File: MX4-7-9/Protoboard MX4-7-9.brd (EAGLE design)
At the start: 82.7 x 59.4 mm, 444 parts, among them J1 DCJ0202

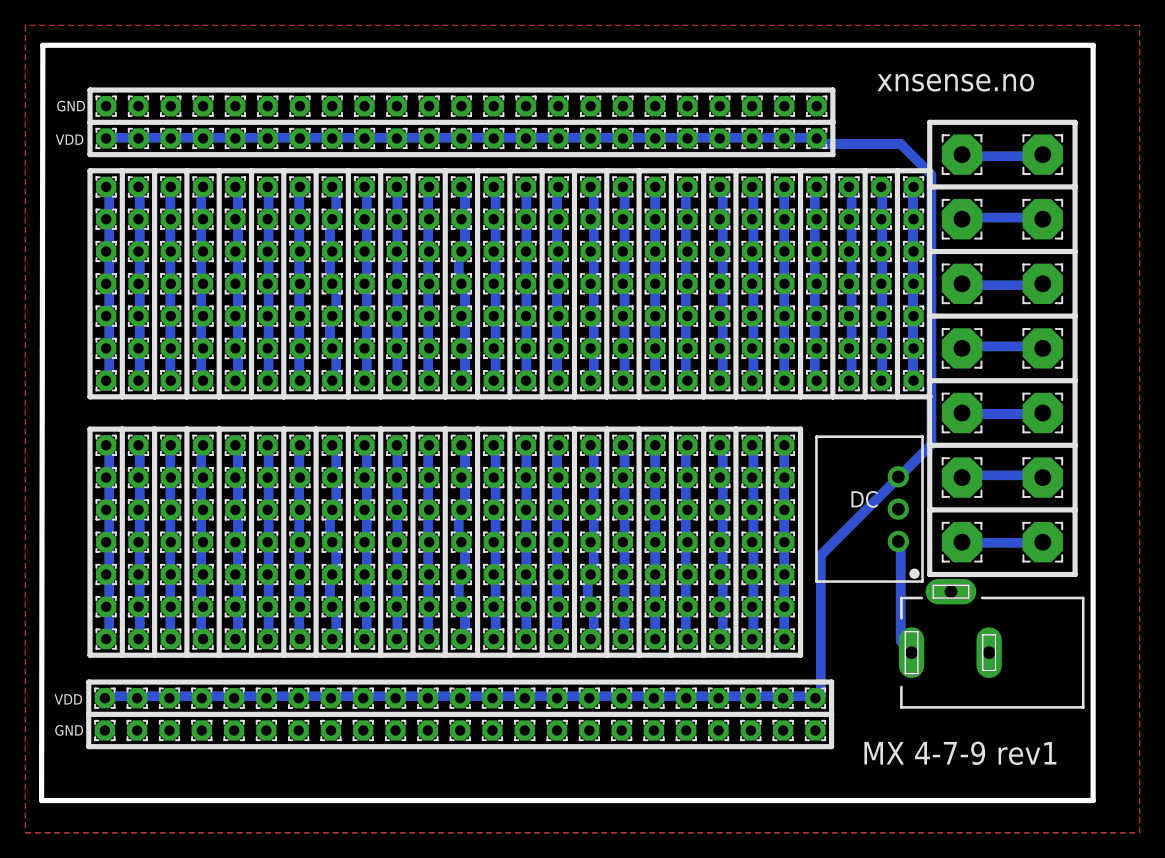
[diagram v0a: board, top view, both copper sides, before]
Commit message: Adjusted Polygon
Adjusted Polygon on all boxes. Changed length on MX-4-7-6 to fit the
box, it was 2mm to long.
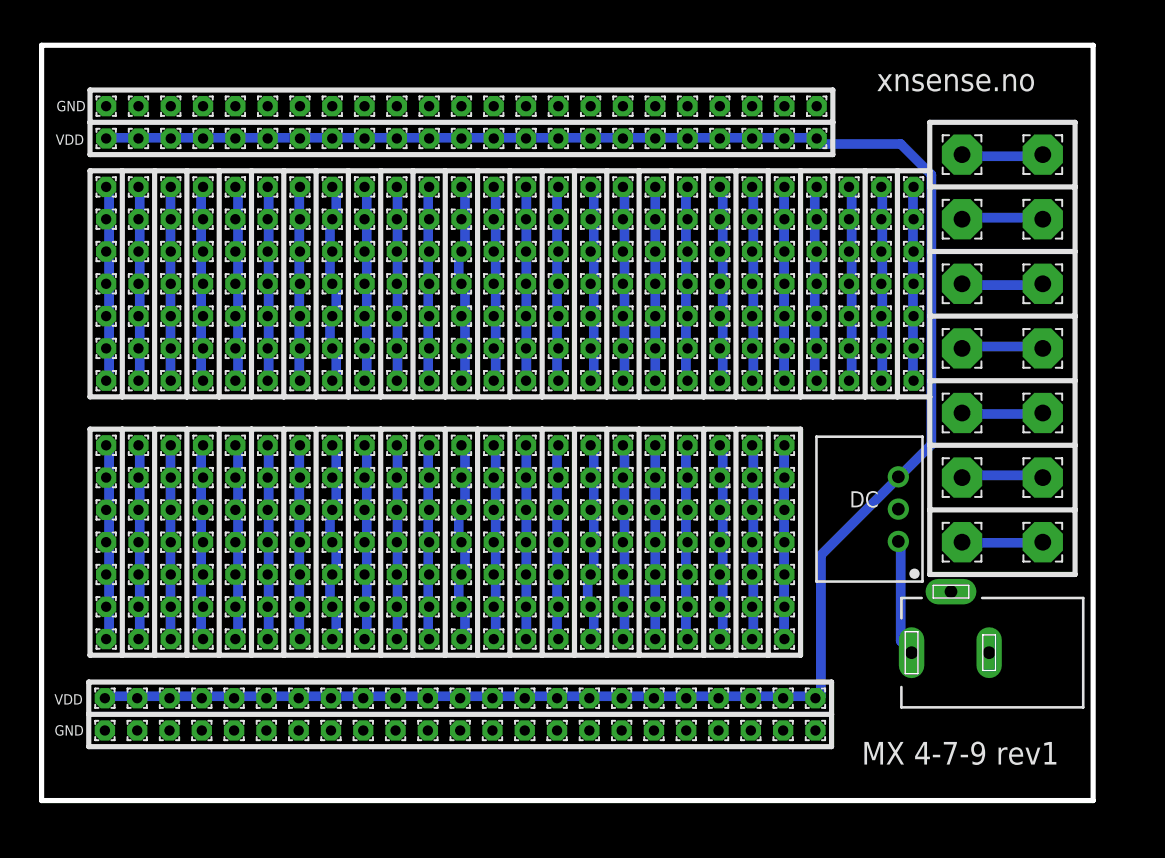
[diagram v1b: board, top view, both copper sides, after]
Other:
- outline, holes or cut-outs redrawn
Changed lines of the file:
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@@
 <?xml version="1.0" encoding="utf-8"?>
 <!DOCTYPE eagle SYSTEM "eagle.dtd">
-<eagle version="7.6.0">
+<eagle version="7.7.0">
 <drawing>
 <settings>
@@
 <setting verticaltext="up"/>
 </settings>
-<grid distance="1.27" unitdist="mm" unit="mm" style="dots" multiple="1" display="yes" altdistance="0.1" altunitdist="mm" altunit="mm"/>
+<grid distance="1.27" unitdist="mm" unit="mil" style="dots" multiple="1" display="yes" altdistance="25" altunitdist="mil" altunit="mil"/>
 <layers>
 <layer number="1" name="Top" color="4" fill="1" visible="yes" active="yes"/>
@@
 <board>
 <plain>
-<wire x1="0" y1="0" x2="0.1" y2="59.4" width="0.4064" layer="20"/>
+<wire x1="0" y1="0" x2="0" y2="59.4" width="0.4064" layer="20"/>
 <wire x1="0" y1="0" x2="82.7" y2="0" width="0.4064" layer="20"/>
-<wire x1="82.7" y1="59.4" x2="0.1" y2="59.4" width="0.4064" layer="20"/>
+<wire x1="82.7" y1="59.4" x2="0" y2="59.4" width="0.4064" layer="20"/>
 <wire x1="82.7" y1="59.4" x2="82.7" y2="0" width="0.4064" layer="20"/>
 <wire x1="44.45" y1="49.53" x2="44.45" y2="31.75" width="0.4064" layer="25"/>
@@
 <contactref element="DC" pad="2"/>
 <polygon width="0.4064" layer="1">
-<vertex x="-1.27" y="60.96"/>
-<vertex x="-1.27" y="-2.54"/>
-<vertex x="86.36" y="-2.54"/>
-<vertex x="86.36" y="60.96"/>
+<vertex x="0" y="59.4"/>
+<vertex x="0" y="0"/>
+<vertex x="82.7" y="0"/>
+<vertex x="82.7" y="59.4"/>
 </polygon>
 <contactref element="PAD27" pad="1"/>

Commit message: Update to rev2
Updated to Pin headers instead of single wire pads
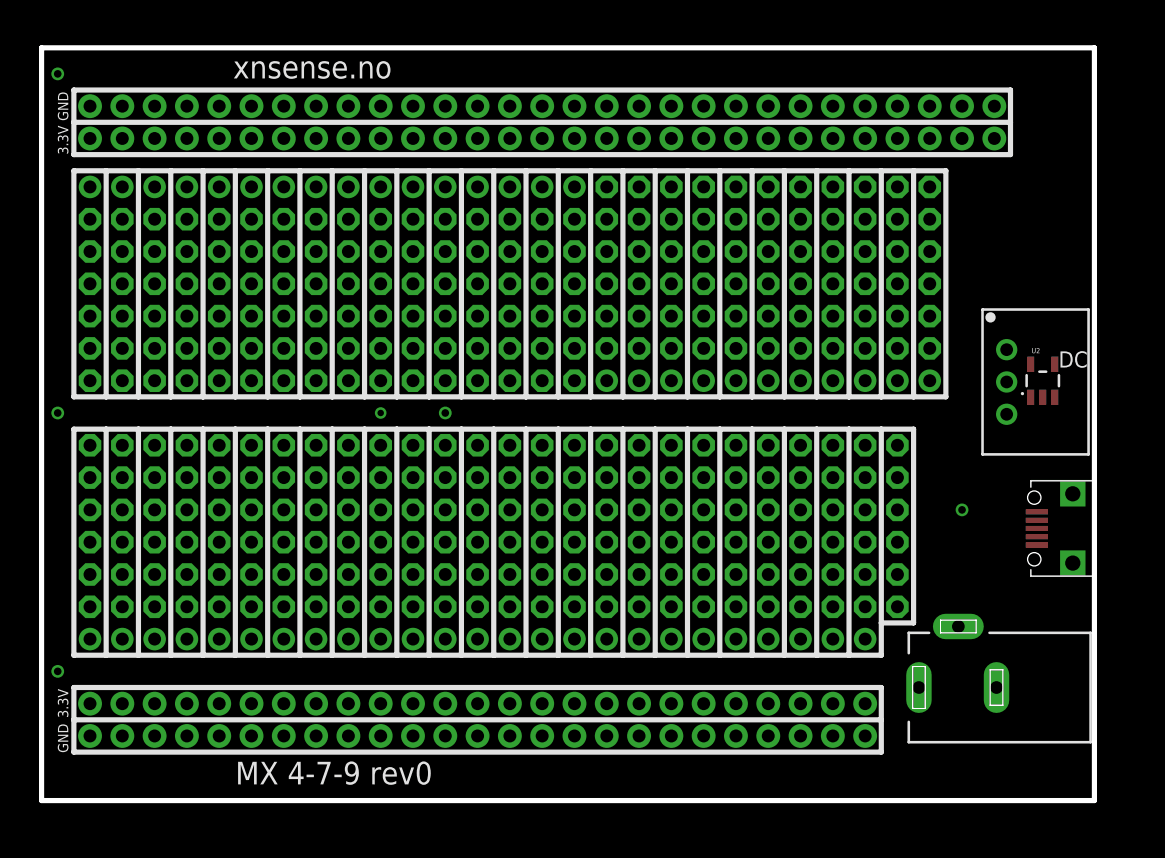
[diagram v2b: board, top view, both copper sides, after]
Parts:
- removed PAD1, PAD10, PAD100, PAD101, PAD102, PAD103, PAD104, PAD105, PAD106, PAD107, PAD108, PAD109, PAD11, PAD110, PAD111, PAD112, PAD113, PAD114, PAD115, PAD116, PAD117, PAD118, PAD119, PAD12, PAD120, PAD121, PAD122, PAD123, PAD124, PAD125, PAD126, PAD127, PAD128, PAD129, PAD13, PAD130, PAD131, PAD132, PAD133, PAD134, PAD135, PAD136, PAD137, PAD138, PAD139, PAD14, PAD140, PAD141, PAD142, PAD143, PAD144, PAD145, PAD146, PAD147, PAD148, PAD149, PAD15, PAD150, PAD151, PAD152, PAD153, PAD154, PAD155, PAD156, PAD157, PAD158, PAD159, PAD16, PAD160, PAD161, PAD162, PAD163, PAD164, PAD165, PAD166, PAD167, PAD168, PAD169, PAD17, PAD170, PAD171, PAD172, PAD173, PAD174, PAD175, PAD176, PAD177, PAD178, PAD179, PAD18, PAD180, PAD181, PAD182, PAD183, PAD184, PAD185, PAD186, PAD187, PAD188, PAD189, PAD19, PAD190, PAD191, PAD192, PAD193, PAD194, PAD195, PAD196, PAD197, PAD198, PAD199, PAD2, PAD20, PAD200, PAD201, PAD202, PAD203, PAD204, PAD205, PAD206, PAD207, PAD208, PAD209, PAD21, PAD210, PAD211, PAD212, PAD213, PAD214, PAD215, PAD216, PAD217, PAD218, PAD219, PAD22, PAD220, PAD221, PAD222, PAD223, PAD224, PAD225, PAD226, PAD227, PAD228, PAD229, PAD23, PAD230, PAD231, PAD232, PAD233, PAD234, PAD235, PAD236, PAD237, PAD238, PAD239, PAD24, PAD240, PAD25, PAD26, PAD260, PAD261, PAD262, PAD263, PAD264, PAD265, PAD266, PAD269, PAD27, PAD270, PAD271, PAD272, PAD273, PAD274, PAD275, PAD276, PAD277, PAD278, PAD279, PAD28, PAD280, PAD281, PAD282, PAD283, PAD284, PAD285, PAD286, PAD287, PAD288, PAD289, PAD29, PAD290, PAD291, PAD292, PAD293, PAD294, PAD295, PAD296, PAD297, PAD298, PAD299, PAD3, PAD30, PAD300, PAD301, PAD302, PAD303, PAD304, PAD305, PAD306, PAD307, PAD308, PAD309, PAD31, PAD310, PAD311, PAD312, PAD313, PAD314, PAD315, PAD316, PAD317, PAD318, PAD319, PAD32, PAD320, PAD321, PAD322, PAD323, PAD324, PAD325, PAD326, PAD327, PAD328, PAD329, PAD33, PAD330, PAD331, PAD332, PAD333, PAD334, PAD335, PAD336, PAD337, PAD338, PAD339, PAD34, PAD340, PAD341, PAD342, PAD343, PAD344, PAD345, PAD346, PAD347, PAD348, PAD349, PAD35, PAD350, PAD351, PAD352, PAD353, PAD354, PAD355, PAD356, PAD357, PAD358, PAD359, PAD36, PAD360, PAD361, PAD362, PAD363, PAD364, PAD365, PAD366, PAD367, PAD368, PAD369, PAD37, PAD370, PAD371, PAD372, PAD373, PAD374, PAD375, PAD376, PAD377, PAD378, PAD379, PAD38, PAD380, PAD381, PAD382, PAD383, PAD384, PAD385, PAD386, PAD387, PAD388, PAD389, PAD39, PAD390, PAD391, PAD392, PAD393, PAD394, PAD395, PAD4, PAD40, PAD41, PAD414, PAD415, PAD416, PAD42, PAD420, PAD421, PAD422, PAD423, PAD424, PAD425, PAD426, PAD427, PAD428, PAD429, PAD43, PAD430, PAD431, PAD432, PAD433, PAD434, PAD435, PAD436, PAD437, PAD438, PAD439, PAD44, PAD440, PAD441, PAD442, PAD443, PAD444, PAD445, PAD446, PAD447, PAD448, PAD449, PAD45, PAD450, PAD451, PAD452, PAD453, PAD454, PAD455, PAD456, PAD457, PAD458, PAD459, PAD46, PAD460, PAD461, PAD462, PAD463, PAD464, PAD465, PAD466, PAD467, PAD468, PAD469, PAD47, PAD470, PAD48, PAD49, PAD5, PAD50, PAD51, PAD52, PAD53, PAD54, PAD55, PAD56, PAD57, PAD58, PAD59, PAD6, PAD60, PAD61, PAD62, PAD63, PAD64, PAD65, PAD66, PAD67, PAD68, PAD69, PAD7, PAD70, PAD71, PAD72, PAD73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: (no value), wirepad:1,6/0,8
- removed PAD471, PAD472, PAD473, PAD474, PAD475, PAD476, PAD477, PAD481, PAD482, PAD483, PAD484, PAD485, PAD486, PAD487: WIREPAD3,17/1,3, wirepad:3,17/1,3
- added J2, J3: (no value), SparkFun-Connectors:1X29_NO_SILK
- added J4, J5: (no value), SparkFun-Connectors:1X20_NO_SILK_KIT
- added J6, J7: (no value), SparkFun-Connectors:1X05_NO_SILK
- added JP1: USB-RECEPTABLE, daspilker:FCI-10103594-0001LF
- added JP10, JP11, JP12, JP13, JP14, JP15, JP16, JP17, JP18, JP19, JP2, JP20, JP21, JP22, JP23, JP24, JP25, JP26, JP27, JP28, JP29, JP3, JP30, JP31, JP32, JP33, JP4, JP47, JP5, JP6, JP64, JP65, JP66, JP67, JP68, JP69, JP7, JP70, JP71, JP72, JP73, JP74, JP75, JP76, JP77, JP78, JP79, JP8, JP80, JP81, JP82, JP83, JP9: (no value), adafruit:1X06-CLEANBIG
- added JP100, JP101, JP102, JP103, JP104, JP105, JP106, JP107, JP108, JP109, JP34, JP35, JP36, JP37, JP38, JP39, JP40, JP41, JP42, JP43, JP44, JP45, JP46, JP48, JP49, JP50, JP51, JP52, JP53, JP54, JP55, JP56, JP57, JP58, JP59, JP60, JP61, JP62, JP63, JP85, JP86, JP87, JP88, JP89, JP90, JP91, JP92, JP93, JP96, JP97, JP98, JP99: (no value), adafruit:1X01-CLEANBIG
- added U2: (no value), SparkFun-PowerIC:SOT23-5
- moved DC 13.1 mm to (75.9, 32.9), turned to 270 degrees
- moved J1 2.80 mm to (72.1, 8.89)
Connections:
- removed net N$25: PAD104.1, PAD105.1, PAD113.1, PAD114.1, PAD87.1, PAD95.1, PAD96.1
- removed net N$40: PAD377.1, PAD378.1, PAD379.1, PAD380.1, PAD381.1, PAD382.1, PAD383.1
- removed net N$45: PAD185.1, PAD186.1, PAD194.1, PAD195.1, PAD203.1, PAD204.1, PAD212.1
- removed net N$60: PAD375.1, PAD376.1, PAD384.1, PAD390.1, PAD395.1, PAD414.1, PAD415.1
- removed net N$61: PAD416.1, PAD420.1, PAD437.1, PAD438.1, PAD457.1, PAD458.1, PAD463.1
- removed net N$62: PAD464.1, PAD465.1, PAD466.1, PAD467.1, PAD468.1, PAD469.1, PAD470.1
- removed net N$63: PAD471.1, PAD487.1
- removed net N$64: PAD472.1, PAD486.1
- removed net N$65: PAD473.1, PAD485.1
- removed net N$66: PAD474.1, PAD484.1
- removed net N$67: PAD475.1, PAD483.1
- removed net N$68: PAD476.1, PAD482.1
- removed net N$69: PAD477.1, PAD481.1
- new net N$2: JP31.1, JP31.2, JP31.3, JP31.4, JP31.5, JP31.6, JP96.1
- new net N$46: JP106.1, JP70.1, JP70.2, JP70.3, JP70.4, JP70.5, JP70.6
- new net N$47: JP107.1, JP71.1, JP71.2, JP71.3, JP71.4, JP71.5, JP71.6
- new net N$48: JP108.1, JP72.1, JP72.2, JP72.3, JP72.4, JP72.5, JP72.6
- new net N$52: JP76.1, JP76.2, JP76.3, JP76.4, JP76.5, JP76.6, JP87.1
- new net N$53: JP77.1, JP77.2, JP77.3, JP77.4, JP77.5, JP77.6, JP88.1
- new net N$54: JP78.1, JP78.2, JP78.3, JP78.4, JP78.5, JP78.6, JP89.1
- new net N$55: JP79.1, JP79.2, JP79.3, JP79.4, JP79.5, JP79.6, JP90.1
- new net N$56: JP80.1, JP80.2, JP80.3, JP80.4, JP80.5, JP80.6, JP91.1
- new net N$57: JP81.1, JP81.2, JP81.3, JP81.4, JP81.5, JP81.6, JP92.1
- new net N$58: JP82.1, JP82.2, JP82.3, JP82.4, JP82.5, JP82.6, JP93.1
- net GND: now also J2.1, J2.10, J2.11, J2.12, J2.13, J2.14, J2.15, J2.16, J2.17, J2.18, J2.19, J2.2, J2.20, J2.21, J2.22, J2.23, J2.24, J2.25, J2.26, J2.27, J2.28, J2.29, J2.3, J2.4, J2.5, J2.6, J2.7, J2.8, J2.9, J4.1, J4.10, J4.11, J4.12, J4.13, J4.14, J4.15, J4.16, J4.17, J4.18, J4.19, J4.2, J4.20, J4.3, J4.4, J4.5, J4.6, J4.7, J4.8, J4.9, J6.1, J6.2, J6.3, J6.4, J6.5, JP1.5, U2.2; no longer PAD17.1, PAD22.1, PAD23.1, PAD24.1, PAD25.1, PAD26.1, PAD27.1, PAD276.1, PAD277.1, PAD28.1, PAD285.1, PAD286.1, PAD29.1, PAD30.1, PAD31.1, PAD32.1, PAD326.1, PAD327.1, PAD328.1, PAD329.1, PAD33.1, PAD330.1, PAD331.1, PAD339.1, PAD36.1, PAD38.1, PAD4.1, PAD421.1, PAD422.1, PAD423.1, PAD424.1, PAD425.1, PAD426.1, PAD427.1, PAD428.1, PAD429.1, PAD430.1, PAD431.1, PAD432.1, PAD433.1, PAD434.1, PAD435.1, PAD436.1, PAD439.1, PAD440.1, PAD441.1
- net N$1: now also JP2.1, JP2.2, JP2.3, JP2.4, JP2.5, JP2.6, JP48.1; no longer PAD391.1, PAD392.1, PAD393.1, PAD394.1, PAD42.1, PAD43.1, PAD44.1
- net N$10: now also JP54.1, JP9.1, JP9.2, JP9.3, JP9.4, JP9.5, JP9.6; no longer PAD106.1, PAD107.1, PAD108.1, PAD109.1, PAD110.1, PAD111.1, PAD112.1
- net N$11: now also JP10.1, JP10.2, JP10.3, JP10.4, JP10.5, JP10.6, JP55.1; no longer PAD115.1, PAD116.1, PAD117.1, PAD118.1, PAD119.1, PAD120.1, PAD121.1
- net N$12: now also JP11.1, JP11.2, JP11.3, JP11.4, JP11.5, JP11.6, JP56.1; no longer PAD124.1, PAD125.1, PAD126.1, PAD127.1, PAD128.1, PAD129.1, PAD130.1
- net N$13: now also JP12.1, JP12.2, JP12.3, JP12.4, JP12.5, JP12.6, JP57.1; no longer PAD133.1, PAD134.1, PAD135.1, PAD136.1, PAD137.1, PAD138.1, PAD139.1
- net N$14: now also JP13.1, JP13.2, JP13.3, JP13.4, JP13.5, JP13.6, JP58.1; no longer PAD142.1, PAD143.1, PAD144.1, PAD145.1, PAD146.1, PAD147.1, PAD148.1
- net N$15: now also JP14.1, JP14.2, JP14.3, JP14.4, JP14.5, JP14.6, JP59.1; no longer PAD151.1, PAD152.1, PAD153.1, PAD154.1, PAD155.1, PAD156.1, PAD157.1
- net N$16: now also JP15.1, JP15.2, JP15.3, JP15.4, JP15.5, JP15.6, JP60.1; no longer PAD160.1, PAD161.1, PAD162.1, PAD163.1, PAD164.1, PAD165.1, PAD166.1
- net N$17: now also JP16.1, JP16.2, JP16.3, JP16.4, JP16.5, JP16.6, JP61.1; no longer PAD169.1, PAD170.1, PAD171.1, PAD172.1, PAD173.1, PAD174.1, PAD175.1
- net N$18: now also JP4.1, JP4.2, JP4.3, JP4.4, JP4.5, JP4.6, JP62.1; no longer PAD178.1, PAD179.1, PAD180.1, PAD181.1, PAD182.1, PAD183.1, PAD184.1
- net N$19: now also JP17.1, JP17.2, JP17.3, JP17.4, JP17.5, JP17.6, JP63.1; no longer PAD187.1, PAD188.1, PAD189.1, PAD190.1, PAD191.1, PAD192.1, PAD193.1
- net N$20: now also JP18.1, JP18.2, JP18.3, JP18.4, JP18.5, JP18.6, JP34.1; no longer PAD196.1, PAD197.1, PAD198.1, PAD199.1, PAD200.1, PAD201.1, PAD202.1
- net N$21: now also JP19.1, JP19.2, JP19.3, JP19.4, JP19.5, JP19.6, JP35.1; no longer PAD205.1, PAD206.1, PAD207.1, PAD208.1, PAD209.1, PAD210.1, PAD211.1
- net N$22: now also JP20.1, JP20.2, JP20.3, JP20.4, JP20.5, JP20.6, JP36.1; no longer PAD214.1, PAD215.1, PAD216.1, PAD217.1, PAD218.1, PAD219.1, PAD220.1
- net N$23: now also JP47.1, JP47.2, JP47.3, JP47.4, JP47.5, JP47.6, JP99.1; no longer PAD66.1, PAD67.1, PAD68.1, PAD69.1, PAD70.1, PAD71.1, PAD72.1
- net N$24: now also JP100.1, JP64.1, JP64.2, JP64.3, JP64.4, JP64.5, JP64.6; no longer PAD73.1, PAD74.1, PAD75.1, PAD76.1, PAD77.1, PAD78.1, PAD86.1
- net N$26: now also JP101.1, JP65.1, JP65.2, JP65.3, JP65.4, JP65.5, JP65.6; no longer PAD122.1, PAD123.1, PAD131.1, PAD132.1, PAD140.1, PAD141.1, PAD149.1
- net N$27: now also JP21.1, JP21.2, JP21.3, JP21.4, JP21.5, JP21.6, JP37.1; no longer PAD260.1, PAD261.1, PAD262.1, PAD263.1, PAD264.1, PAD265.1, PAD266.1
- net N$28: now also JP22.1, JP22.2, JP22.3, JP22.4, JP22.5, JP22.6, JP38.1; no longer PAD269.1, PAD270.1, PAD271.1, PAD272.1, PAD273.1, PAD274.1, PAD275.1
- net N$29: now also JP23.1, JP23.2, JP23.3, JP23.4, JP23.5, JP23.6, JP39.1; no longer PAD278.1, PAD279.1, PAD280.1, PAD281.1, PAD282.1, PAD283.1, PAD284.1
- net N$3: now also JP32.1, JP32.2, JP32.3, JP32.4, JP32.5, JP32.6, JP97.1; no longer PAD1.1, PAD2.1, PAD3.1, PAD34.1, PAD35.1, PAD37.1, PAD40.1
- net N$30: now also JP24.1, JP24.2, JP24.3, JP24.4, JP24.5, JP24.6, JP40.1; no longer PAD287.1, PAD288.1, PAD289.1, PAD290.1, PAD291.1, PAD292.1, PAD293.1
- net N$31: now also JP25.1, JP25.2, JP25.3, JP25.4, JP25.5, JP25.6, JP41.1; no longer PAD296.1, PAD297.1, PAD298.1, PAD299.1, PAD300.1, PAD301.1, PAD302.1
- net N$32: now also JP26.1, JP26.2, JP26.3, JP26.4, JP26.5, JP26.6, JP42.1; no longer PAD305.1, PAD306.1, PAD307.1, PAD308.1, PAD309.1, PAD310.1, PAD311.1
- net N$33: now also JP27.1, JP27.2, JP27.3, JP27.4, JP27.5, JP27.6, JP43.1; no longer PAD314.1, PAD315.1, PAD316.1, PAD317.1, PAD318.1, PAD319.1, PAD320.1
- net N$34: now also JP102.1, JP66.1, JP66.2, JP66.3, JP66.4, JP66.5, JP66.6; no longer PAD150.1, PAD158.1, PAD159.1, PAD167.1, PAD168.1, PAD176.1, PAD177.1
- net N$35: now also JP28.1, JP28.2, JP28.3, JP28.4, JP28.5, JP28.6, JP44.1; no longer PAD332.1, PAD333.1, PAD334.1, PAD335.1, PAD336.1, PAD337.1, PAD338.1
- net N$36: now also JP29.1, JP29.2, JP29.3, JP29.4, JP29.5, JP29.6, JP45.1; no longer PAD341.1, PAD342.1, PAD343.1, PAD344.1, PAD345.1, PAD346.1, PAD347.1
- net N$37: now also JP30.1, JP30.2, JP30.3, JP30.4, JP30.5, JP30.6, JP46.1; no longer PAD350.1, PAD351.1, PAD352.1, PAD353.1, PAD354.1, PAD355.1, PAD356.1
- net N$38: now also JP103.1, JP67.1, JP67.2, JP67.3, JP67.4, JP67.5, JP67.6; no longer PAD359.1, PAD360.1, PAD361.1, PAD362.1, PAD363.1, PAD364.1, PAD365.1
- net N$39: now also JP104.1, JP68.1, JP68.2, JP68.3, JP68.4, JP68.5, JP68.6; no longer PAD368.1, PAD369.1, PAD370.1, PAD371.1, PAD372.1, PAD373.1, PAD374.1
- net N$4: now also JP33.1, JP33.2, JP33.3, JP33.4, JP33.5, JP33.6, JP98.1; no longer PAD45.1, PAD46.1, PAD47.1, PAD48.1, PAD49.1, PAD50.1, PAD51.1
- net N$41: now also JP105.1, JP69.1, JP69.2, JP69.3, JP69.4, JP69.5, JP69.6; no longer PAD385.1, PAD386.1, PAD387.1, PAD388.1, PAD389.1, PAD39.1, PAD41.1
- net N$49: now also JP109.1, JP73.1, JP73.2, JP73.3, JP73.4, JP73.5, JP73.6; no longer PAD213.1, PAD221.1, PAD222.1, PAD223.1, PAD224.1, PAD225.1, PAD226.1
- net N$5: now also JP3.1, JP3.2, JP3.3, JP3.4, JP3.5, JP3.6, JP49.1; no longer PAD52.1, PAD53.1, PAD54.1, PAD55.1, PAD56.1, PAD57.1, PAD58.1
- net N$50: now also JP74.1, JP74.2, JP74.3, JP74.4, JP74.5, JP74.6, JP85.1; no longer PAD227.1, PAD228.1, PAD229.1, PAD230.1, PAD231.1, PAD232.1, PAD233.1
- net N$51: now also JP75.1, JP75.2, JP75.3, JP75.4, JP75.5, JP75.6, JP86.1; no longer PAD234.1, PAD235.1, PAD236.1, PAD237.1, PAD238.1, PAD239.1, PAD240.1
- net N$59: now also JP83.1, JP83.2, JP83.3, JP83.4, JP83.5, JP83.6; no longer PAD340.1, PAD348.1, PAD349.1, PAD357.1, PAD358.1, PAD366.1, PAD367.1
- net N$6: now also JP5.1, JP5.2, JP5.3, JP5.4, JP5.5, JP5.6, JP50.1; no longer PAD59.1, PAD60.1, PAD61.1, PAD62.1, PAD63.1, PAD64.1, PAD65.1
- net N$7: now also JP51.1, JP6.1, JP6.2, JP6.3, JP6.4, JP6.5, JP6.6; no longer PAD79.1, PAD80.1, PAD81.1, PAD82.1, PAD83.1, PAD84.1, PAD85.1
- net N$8: now also JP52.1, JP7.1, JP7.2, JP7.3, JP7.4, JP7.5, JP7.6; no longer PAD88.1, PAD89.1, PAD90.1, PAD91.1, PAD92.1, PAD93.1, PAD94.1
- net N$9: now also JP53.1, JP8.1, JP8.2, JP8.3, JP8.4, JP8.5, JP8.6; no longer PAD100.1, PAD101.1, PAD102.1, PAD103.1, PAD97.1, PAD98.1, PAD99.1
- net VCC: now also JP1.1, U2.1, U2.3
- net VDD: now also J3.1, J3.10, J3.11, J3.12, J3.13, J3.14, J3.15, J3.16, J3.17, J3.18, J3.19, J3.2, J3.20, J3.21, J3.22, J3.23, J3.24, J3.25, J3.26, J3.27, J3.28, J3.29, J3.3, J3.4, J3.5, J3.6, J3.7, J3.8, J3.9, J5.1, J5.10, J5.11, J5.12, J5.13, J5.14, J5.15, J5.16, J5.17, J5.18, J5.19, J5.2, J5.20, J5.3, J5.4, J5.5, J5.6, J5.7, J5.8, J5.9, J7.1, J7.2, J7.3, J7.4, J7.5, U2.5; no longer PAD10.1, PAD11.1, PAD12.1, PAD13.1, PAD14.1, PAD15.1, PAD16.1, PAD18.1, PAD19.1, PAD20.1, PAD21.1, PAD294.1, PAD295.1, PAD303.1, PAD304.1, PAD312.1, PAD313.1, PAD321.1, PAD322.1, PAD323.1, PAD324.1, PAD325.1, PAD442.1, PAD443.1, PAD444.1, PAD445.1, PAD446.1, PAD447.1, PAD448.1, PAD449.1, PAD450.1, PAD451.1, PAD452.1, PAD453.1, PAD454.1, PAD455.1, PAD456.1, PAD459.1, PAD460.1, PAD461.1, PAD462.1, PAD5.1, PAD6.1, PAD7.1, PAD8.1, PAD9.1
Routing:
- net VDD: track 170.0 -> 0.00 mm
- net N$15: track 17.0 -> 0.00 mm
- net N$21: track 16.8 -> 0.00 mm
- net N$17: track 16.8 -> 0.00 mm
- net N$40: track 16.7 -> 0.00 mm, vias 0 -> 1
- net N$38: track 16.6 -> 0.00 mm
- net N$9: track 16.6 -> 0.00 mm
- net N$49: track 16.6 -> 0.00 mm
- net N$25: track 16.6 -> 0.00 mm, vias 0 -> 2
- net N$4: track 16.4 -> 0.00 mm
- net N$27: track 16.4 -> 0.00 mm
- net N$60: track 16.4 -> 0.00 mm
- net N$11: track 16.4 -> 0.00 mm
- net N$31: track 16.2 -> 0.00 mm
- net N$12: track 16.2 -> 0.00 mm
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- added copper zone on layer 16, net N$45
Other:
- board size 82.7 x 59.4 mm -> 82.8 x 59.2 mm
- board text added: "3.3V"
- board text added: "MX 4-7-9 rev0"
- board text removed: "MX 4-7-9 rev1"
- board text removed: "VDD"

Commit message: Change usb connector
Change to correct usb connecter and moved esp8266 bit more onto the
board.
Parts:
- removed JP1: USB-RECEPTABLE, daspilker:FCI-10103594-0001LF
- added X1: (no value), microbuilder:4UCONN_20329
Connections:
- net GND: now also X1.BASE@1, X1.BASE@2, X1.GND, X1.SPRT@1, X1.SPRT@2, X1.SPRT@3, X1.SPRT@4; no longer JP1.5
- net VCC: now also X1.VBUS; no longer JP1.1
